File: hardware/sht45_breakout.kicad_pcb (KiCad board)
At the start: 2 copper layers, 10.2 x 12.5 mm, 6 parts, among them J1 I2C, U1 SHT45-AD1B-R2

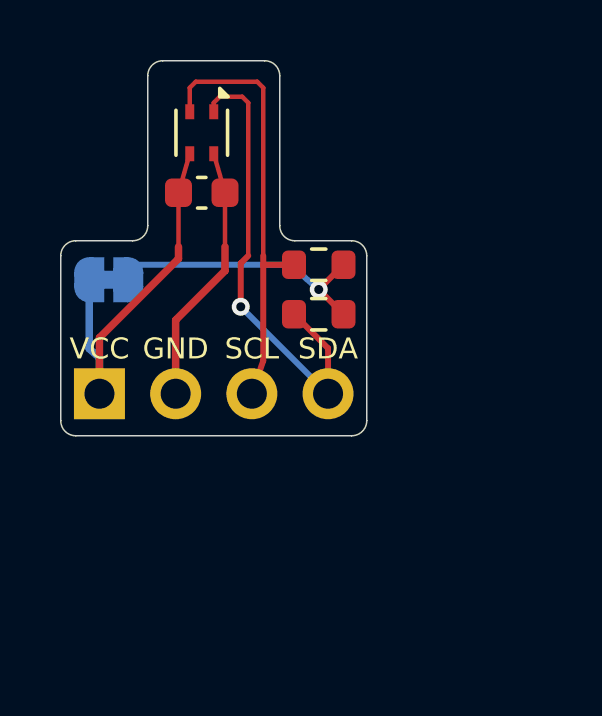
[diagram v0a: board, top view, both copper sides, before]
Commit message: Add JST XH connector and M2 mounting holes, enlarge board to 16 x 19.8 mm
J2 (JST XH B4B-XH-A) sits right below the 2.54 mm header with the same
VCC/GND/SCL/SDA order. Two M2 holes live on ears either side of the sensor
tongue, separated from it by 1.2 mm milled slots so the thermal
decoupling is kept. Schematic gains J2 and H1/H2; DRC and schematic/PCB
net comparison still clean.

Co-Authored-By: Claude Opus 5.5 <noreply@anthropic.com>
Claude-Session: https://claude.ai/code/session_01Cw4qgvdZTYbLFFCGBumb2e
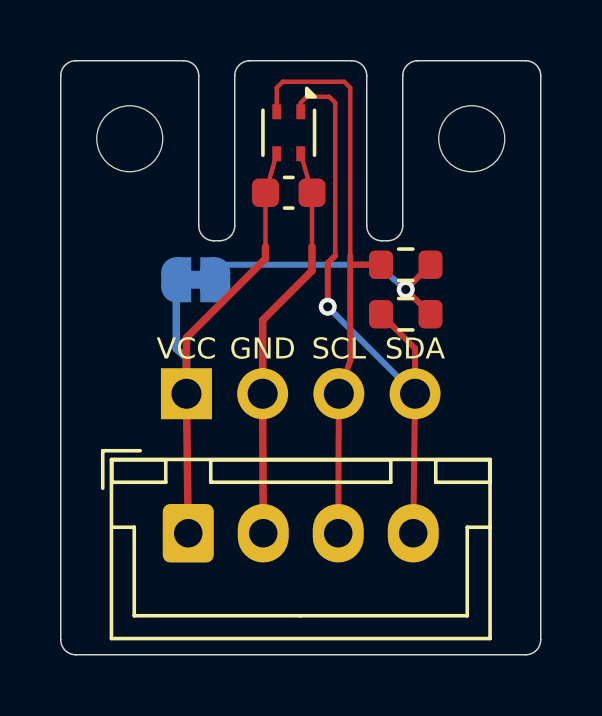
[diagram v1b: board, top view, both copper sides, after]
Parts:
- added H1: M2, MountingHole:MountingHole_2.2mm_M2, F.Cu at (102.3, 102.6)
- added H2: M2, MountingHole:MountingHole_2.2mm_M2, F.Cu at (113.7, 102.6)
- added J2: XH, Connector_JST:JST_XH_B4B-XH-A_1x04_P2.50mm_Vertical, F.Cu at (104.2, 115.8)
- moved JP1 2.90 mm to (104.5, 107.3)
- moved R1 2.90 mm to (111.5, 108.5)
- moved R2 2.90 mm to (111.5, 106.8)
- moved C1 2.90 mm to (107.6, 104.4)
- moved J1 2.90 mm to (104.2, 111.1)
- moved U1 2.90 mm to (107.6, 102.4)
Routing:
- net /SDA: track 15.8 -> 20.4 mm
- net VCC: track 13.1 -> 17.7 mm
- net GND: track 8.73 -> 13.4 mm
- net /SCL: track 14.7 -> 19.4 mm
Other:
- board size 10.2 x 12.5 mm -> 16 x 19.8 mm
